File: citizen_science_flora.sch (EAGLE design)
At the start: 13 parts, among them IC1 W25Q64JVXGIQ, U1 RP2350A

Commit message: Update citizen_science_flora.sch
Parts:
- added !BOOT, RESET: MOMENTARY-SWITCH-SPST-SMD-4.6X2.8MM, SparkFun-Switches:MOMENTARY-SWITCH-SPST-SMD-4.6X2.8MM
- added C11, C12, C14: 4.7uF, SparkFun-Capacitors:4.7UF-0402_TIGHT-6.3V-20%-X5R
- added C13, C15, C16, C17, C25, C26, C27, C28, C29: 0.1uF, SparkFun-Capacitors:0.1UF-0402T-16V-10%-X7R-WE
- added C18, C19: 15pF, SparkFun-Capacitors:15PF-0402-50V-5%
- added C20, C23, C24: 10uF, SparkFun-Capacitors:10UF-0402T-6.3V-20%
- added C21, C22: 0.1uF, SparkFun-Capacitors:0.1UF-0402-6.3V-10%-X7R
- added J1: SM03B-SRSS-TB(LF)(SN), SM03B-SRSS-TB_LF__SN_:SM03B-SRSS-TB(LF)(SN)
- added J2: TYPE-C-31-M-12, TYPE-C-31-M-12:TYPE-C-31-M-12
- added J3: (no value), SparkFun-Connectors:QWIIC_CONNECTORJS-1MM
- added L1: 3.3µH, SparkFun-Coils:INDUCTOR-0805-3.3UH
- added L2: LQW18AN2N2D10D, LQW18AN2N2D10D:LQW18AN2N2D10D
- added R10, R9: 5.1k, SparkFun-Resistors:5.1KOHM-0402-1/16W-1%
- added R11, R12: 2.2K, SparkFun-Resistors:2.2KOHM-0402-1/16W-1%
- added R2, R6, R8: 1K, SparkFun-Resistors:1KOHM-0402-1/16W-1%
- added R3, R4: 27, SparkFun-Resistors:27OHM
- added R5: (no value), SparkFun-Resistors:RESISTOR0402
- added R7: 10k, SparkFun-Resistors:10KOHM-0402-1/16W-1%
- added TP1, TP2, TP3: TPB1,27, testpad:TPB1,27
- added U$1: TF-123-ARP9HXX, xunpu_tf123:TF-123-ARP9HXX
- added U2: APS6404L-3SQR-ZR, RP2350A:APS6404L-3SQR-ZR
- added U3: ESP32-C3-MINI-1-N4, ESP32-C3-MINI-1-N4:ESP32-C3-MINI-1-N4
- added U4: MIC5504-3.3YM5-T5, MIC5504-3.3YM5-T5:MIC5504-3.3YM5-T5
- added U5: BME690, BME690:BME690
- added U6: ADM3260ARSZ, ADM3260ARSZ:ADM3260ARSZ
- added U7: ENS210-LQFM, ENS210-LQFM:ENS210-LQFM
- added Y1: 12MHz, SparkFun-Clocks:CRYSTAL-GROUNDEDSMD-3.2X2.5
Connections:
- new net !FLASH_CS: R7.2, U1.GPIO0, U2.!CE!
- new net !QSPI_CS: IC1.!CS, R5.1, R6.2, U1.QSPI_!CS!
- new net !RESET: RESET.1, U1.RUN
- new net !USB_BOOT: !BOOT.2, R6.1
- new net 1.1V: C11.1, C13.1, C14.1, C15.1, L1.2, U1.DVDD, U1.VREG_FB
- new net ESP32_RX: U1.GPIO4, U3.RXD0
- new net ESP32_TX: U1.GPIO5, U3.TXD0
- new net N$10: J2.CC2, R9.2
- new net N$11: C21.1, J2.VBUS, L2.1
- new net N$2: L1.1, U1.VREG_LX
- new net N$3: R2.1, RESET.2
- new net N$4: C18.1, R8.1, Y1.2
- new net N$5: R3.2, U1.USB_D+
- new net N$6: R4.2, U1.USB_D-
- new net N$7: C19.1, U1.XIN, Y1.1
- new net N$8: R8.2, U1.XOUT
- new net N$9: J2.CC1, R10.2
- new net QSPI_CLK: IC1.CLK, U1.QSPI_SCLK, U2.SCLK
- new net SCL: J3.4, R12.1, U1.GPIO25, U5.SCK, U7.SCL
- new net SDA: J3.3, R11.1, U1.GPIO24, U5.SDI, U7.SDA
- new net SIO0: IC1.DI(IO0), U1.QSPI_SD0, U2.SI/SIO0
- new net SIO1: IC1.DO(IO1), U1.QSPI_SD1, U2.SO/SIO1
- new net SIO2: IC1.!WP(IO2), U1.QSPI_SD2, U2.SIO2
- new net SIO3: IC1.!HOLD_OR_!RESET_(IO3), U1.QSPI_SD3, U2.SIO3
- new net SWCLK: J1.1, U1.SWCLK
- new net SWDIO: J1.3, U1.SWDIO
- new net USB_N: J2.DN1, J2.DN2, R4.1
- new net USB_P: J2.DP1, J2.DP2, R3.1
- new net V_USB: C22.1, C23.2, L2.2, TP1.TP, U4.EN, U4.VIN
- net 3.3V: now also C12.1, C16.1, C17.2, C20.1, C24.2, C25.1, C26.1, C27.1, C28.1, C29.1, IC1.VCC, J3.2, R11.2, R12.2, R5.2, R7.1, TP3.TP, U$1.VDD, U2.VDD, U3.3V3, U4.VOUT, U5.CSB, U5.VDD, U5.VDDIO, U7.VDD
- net GND: now also !BOOT.1, C11.2, C12.2, C13.2, C14.2, C15.2, C16.2, C17.1, C18.2, C19.2, C20.2, C21.2, C22.2, C23.1, C24.1, C25.2, C26.2, C27.2, C28.2, C29.2, J1.2, J1.SHIELD, J2.GND, J2.SHIELD, J3.1, R10.1, R2.2, R9.1, TP2.TP, U$1.GND, U2.VSS, U3.GND, U4.GND, U5.GND, U5.SDO, U7.VSS, Y1.GND
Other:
- note added: "BOOT pin"
- note added: "Debug"
- note added: "External Flash"
- note added: "MicroSD Card"
- note added: "PSRAM"
- note added: "Qwiic/I2C"
- note added: "RESET Pin"
- note added: "RP2350A"
- note added: "Sensors"
- note added: "Slave Address: 0x43"

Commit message: Update citizen_science_flora.sch
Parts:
- added R13: 10k, SparkFun-Resistors:10KOHM-0402-1/16W-1%
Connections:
- new net !ESP32_BOOT: U3.IO9
- new net !ESP32_RST: U3.EN
- new net CMD: U$1.CMD, U1.GPIO15
- new net DAT0: U$1.DAT0, U1.GPIO12
- new net DAT1: U$1.DAT1, U1.GPIO11
- new net DAT2: U$1.DAT2, U1.GPIO10
- new net DAT3: U$1.CD/DAT3, U1.GPIO13
- new net ESP32_CS: U3.IO10
- new net ESP32_HANDSHAKE: U3.IO3
- new net ESP32_MISO: U3.IO2
- new net ESP32_MOSI: U3.IO7
- new net ESP32_SCK: U3.IO6
- new net N$12: R13.1, U3.IO8
- new net SD_CLK: U$1.CLK, U1.GPIO14
- new net SWITCH: U$1.SWITCH, U1.GPIO9
- net 3.3V: now also R13.2
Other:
- note added: "ESP32 Co-Processor"

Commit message: Update citizen_science_flora.sch
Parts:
- added C30: 0.1uF, SparkFun-Capacitors:0.1UF-0402-6.3V-10%-X7R
- added C31, C35, C37: 10uF, SparkFun-Capacitors:10UF-0402T-6.3V-20%
- added C32: 1.0uF, SparkFun-Capacitors:1.0UF-0402-16V-10%
- added C33: 1nF, SparkFun-Capacitors:1.0NF/1000PF-0402-25V-10%-X7R
- added C34, C36, C38, C39, C40, C41: 0.1uF, SparkFun-Capacitors:0.1UF-0402T-16V-10%-X7R-WE
- added J4, J5: 60312202114511, 60312202114511:60312202114511
- added L3: MA5532-AE, MA5532-AE:MA5532-AE
- added R14, R15: 1K, SparkFun-Resistors:1KOHM-0402-1/16W-1%
- added R16, R17: 100, SparkFun-Resistors:100OHM-0402-TIGHT-1/16W-1%
- added R18, R20: 10K, SparkFun-Resistors:10KOHM-0402-1/10W-0.1%
- added R19: 16.9K, SparkFun-Resistors:RESISTOR0402
- added R21, R22: 2.2K, SparkFun-Resistors:2.2KOHM-0402-1/16W-1%
- added U$2, U$3: PH-OEM, pH-OEM:PH-OEM
- added U8: SFH6325-X017TEL0631, SFH6325-X017T:SFH6325-X017TEL0631
- added U9: AS3935-BQFT, AS3935-BQFT:AS3935-BQFT
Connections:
- new net GND-ISO: C37.2, C38.2, C39.2, C40.1, C41.1, R20.1, U$2.GND, U$3.GND, U6.GNDISO, U8.C1, U8.C2
- new net INT_SOIL: R14.1, U1.GPIO1, U8.C1(VO1)
- new net INT_SOILTEMP: R15.1, U1.GPIO2, U8.C2(VO2)
- new net INT_SOILTEMP_ISO: R16.1, U$3.INT
- new net INT_SOIL_ISO: R17.1, U$2.INT
- new net IRQ_LIGHTNING: U1.GPIO7, U9.IRQ
- new net N$13: R16.2, U8.A2
- new net N$14: R17.2, U8.A1
- new net N$15: C31.1, U9.ACG
- new net N$16: C33.1, L3.2, R18.2, U9.INP
- new net N$17: R19.1, R20.2, U6.VSEL
- new net N$18: J4.1, U$2.PRB
- new net N$19: J4.2, U$2.PRB_GND
- new net N$20: J5.2, U$3.PRB_GND
- new net N$21: J5.1, U$3.PRB
- new net PDIS: U1.GPIO8, U6.PDIS
- new net SCL_ISO: R22.1, U$2.SCL, U6.SCL1
- new net SDA_ISO: R21.1, U$2.SDA, U6.SDA1
- new net VCC-ISO: C37.1, C38.1, C39.1, C40.2, R19.2, R21.2, R22.2, U$2.VCC, U$3.VCC, U6.VDDISO, U6.VISO
- net !ESP32_BOOT: now also U1.GPIO19
- net !ESP32_RST: now also U1.GPIO18
- net 3.3V: now also C30.1, C32.1, C36.2, R14.2, R15.2, U6.VDDP, U8.C(VCC), U9.SI, U9.VDD, U9.VREG
- net ESP32_CS: now also U1.GPIO21
- net ESP32_HANDSHAKE: now also U1.GPIO17
- net ESP32_MISO: now also U1.GPIO20
- net ESP32_MOSI: now also U1.GPIO23
- net ESP32_SCK: now also U1.GPIO22
- net GND: now also C30.2, C31.2, C32.2, C33.2, C34.1, C35.1, C36.1, L3.1, R18.1, U6.GNDP, U8.E(GND), U9.!CS, U9.ADD0, U9.ADD1, U9.EN_VREG, U9.EXP, U9.GND, U9.INN, U9.MISO
- net SCL: now also U6.SCL2, U9.I2CL/SCL
- net SDA: now also U6.SDA2, U9.I2CD/MOSI
- net V_USB: now also C34.2, C35.2, U6.VIN
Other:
- note added: "I2C Isolator"
- note added: "Lightning sensor"
- note added: "Optocoupler"
- note added: "USB Power Supply"

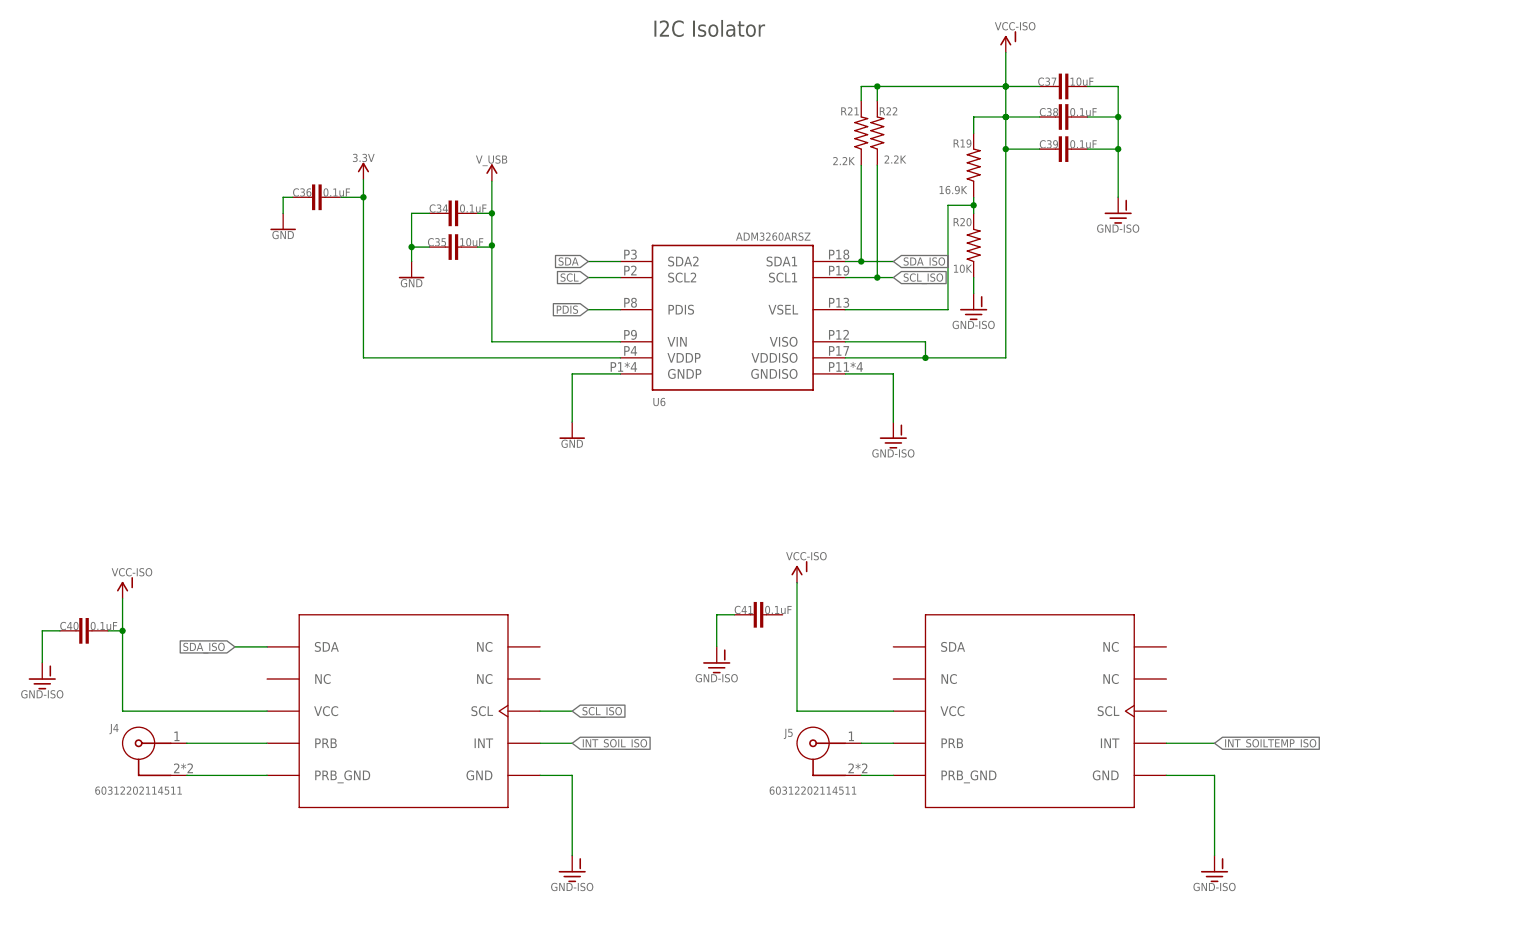
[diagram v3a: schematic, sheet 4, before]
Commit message: Added floral outline
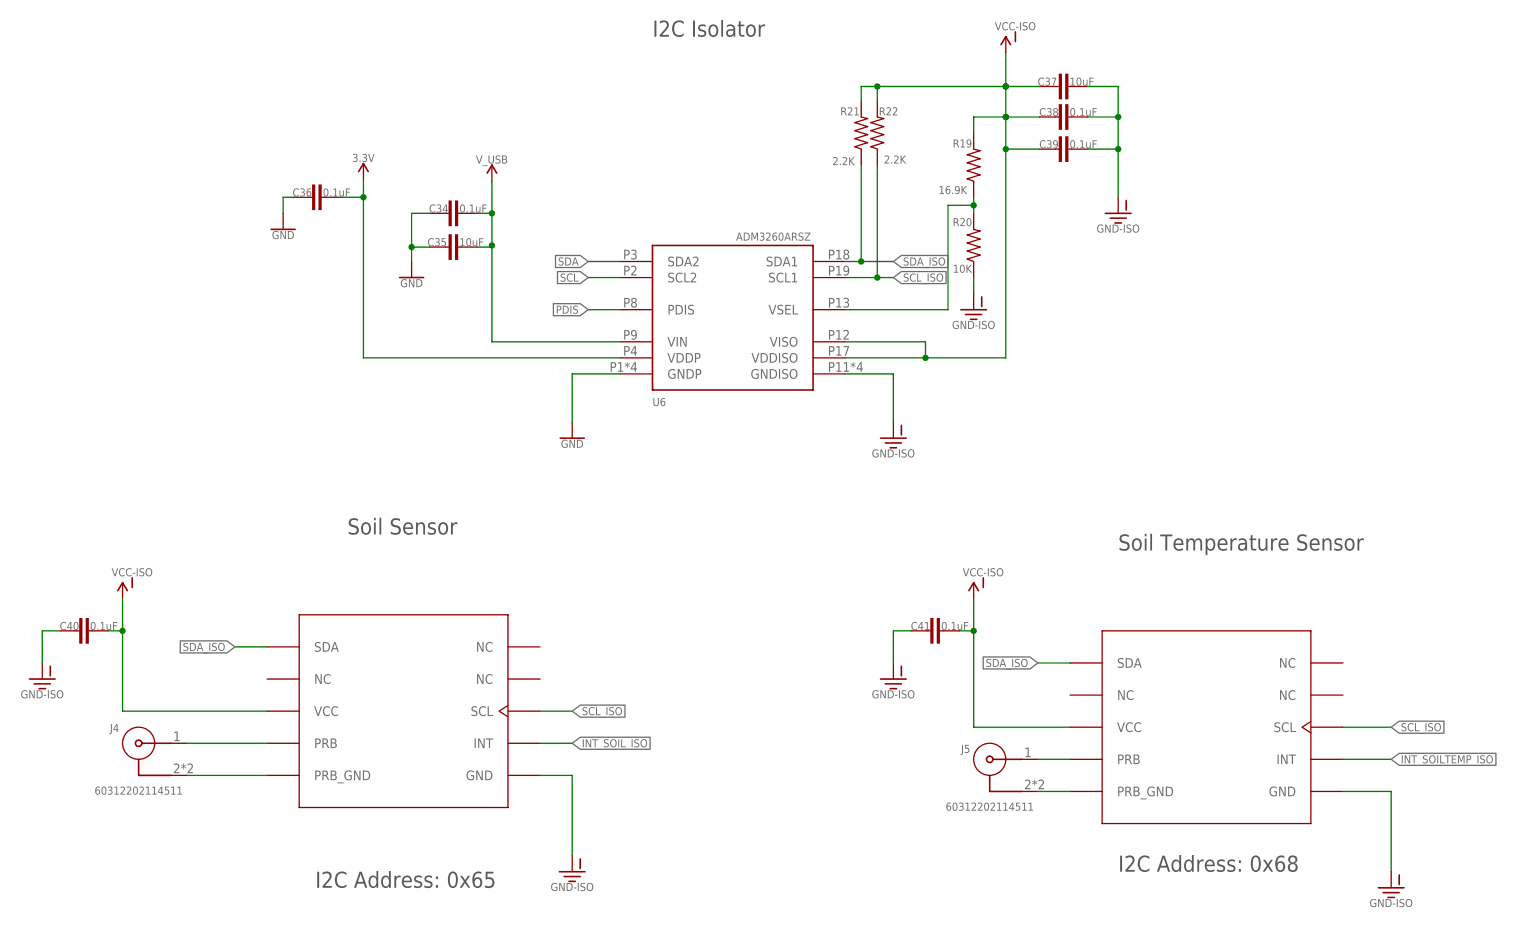
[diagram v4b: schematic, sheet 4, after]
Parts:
- R11: value 2.2K -> DNF
- R12: value 2.2K -> 10K
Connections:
- net 3.3V: now also U9.ADD0, U9.ADD1
- net GND: no longer U9.ADD0, U9.ADD1
- net SCL_ISO: now also U$3.SCL
- net SDA_ISO: now also U$3.SDA
- net VCC-ISO: now also C41.2
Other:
- note added: "I2C Address: 0x65"
- note added: "I2C Address: 0x68"
- note added: "I2C Address: 0x76"
- note added: "Soil Sensor"
- note added: "Soil Temperature Sensor"
- moved on the sheet: C41, J5
